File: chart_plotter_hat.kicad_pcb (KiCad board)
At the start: 4 copper layers, 65 x 56 mm, 37 parts, among them J1 Conn_02x03_Odd_Even, J2 Conn_01x04, J3 40HAT, J4 Conn_01x04, J5 Conn_01x04, J6 Conn_01x02, J7 Conn_01x04, J8 Conn_02x03_Odd_Even, Q1 DMG2305UX, Q2 DMMT5401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

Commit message: Added pulldown R10 on MCU_RUNNING
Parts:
- added R10: 10K, Resistors_SMD:R_0603, F.Cu at (112.0, 84.5)
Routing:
- net MCU_RUNNING: track 31.0 -> 32.3 mm
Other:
- board text added: "12V"
- board text added: "5V"
- board text removed: "+12V"
- board text removed: "+5V"

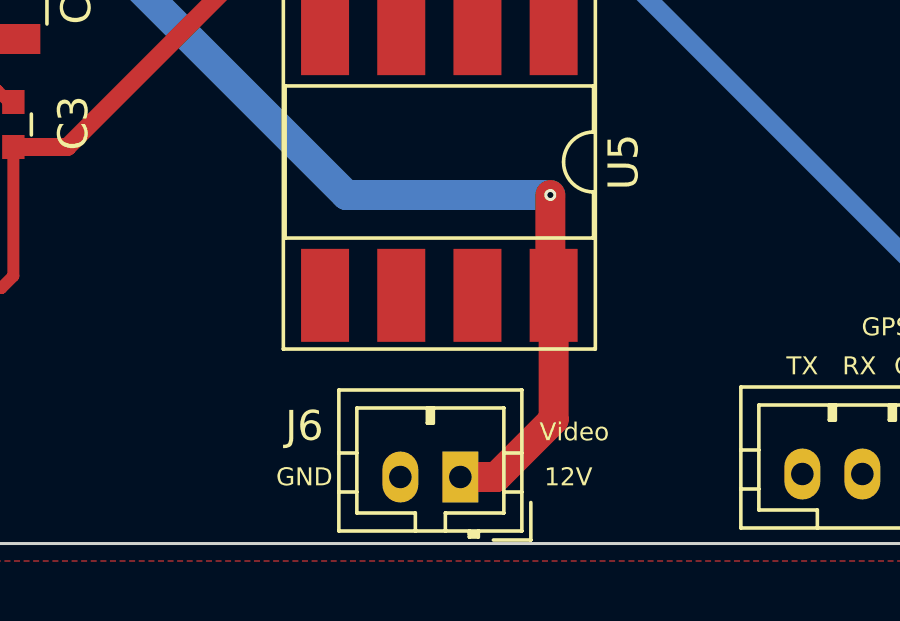
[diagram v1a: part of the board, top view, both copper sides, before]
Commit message: Fixed relay net
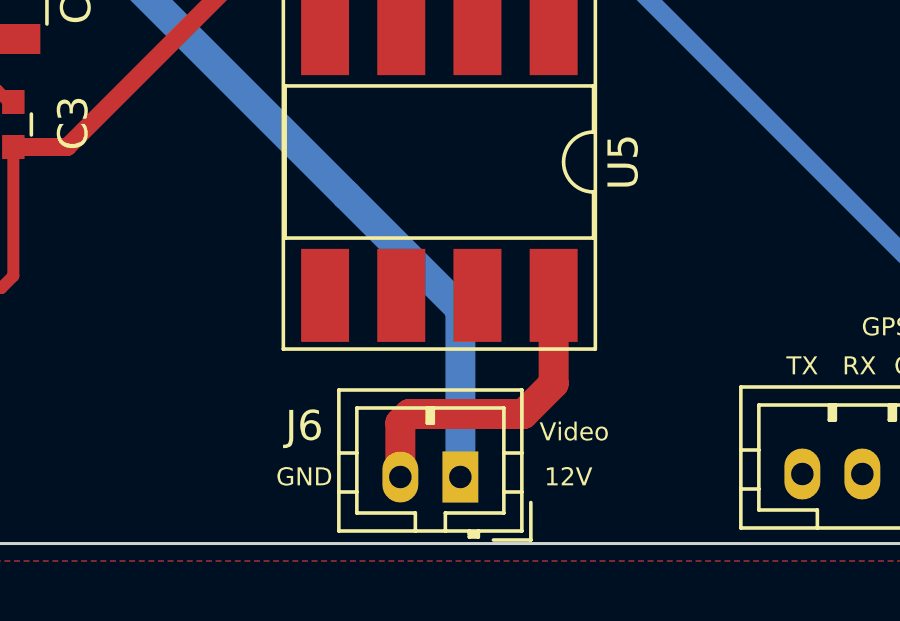
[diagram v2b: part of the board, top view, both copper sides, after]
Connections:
- J6 pad 2: GND -> Net-(J6-Pad2)
- U5 pad 8: +12V -> Net-(J6-Pad2)
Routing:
- net Net-(J6-Pad2): track 0.00 -> 10.6 mm
- net +12V: track 67.7 -> 60.4 mm, vias 2 -> 1

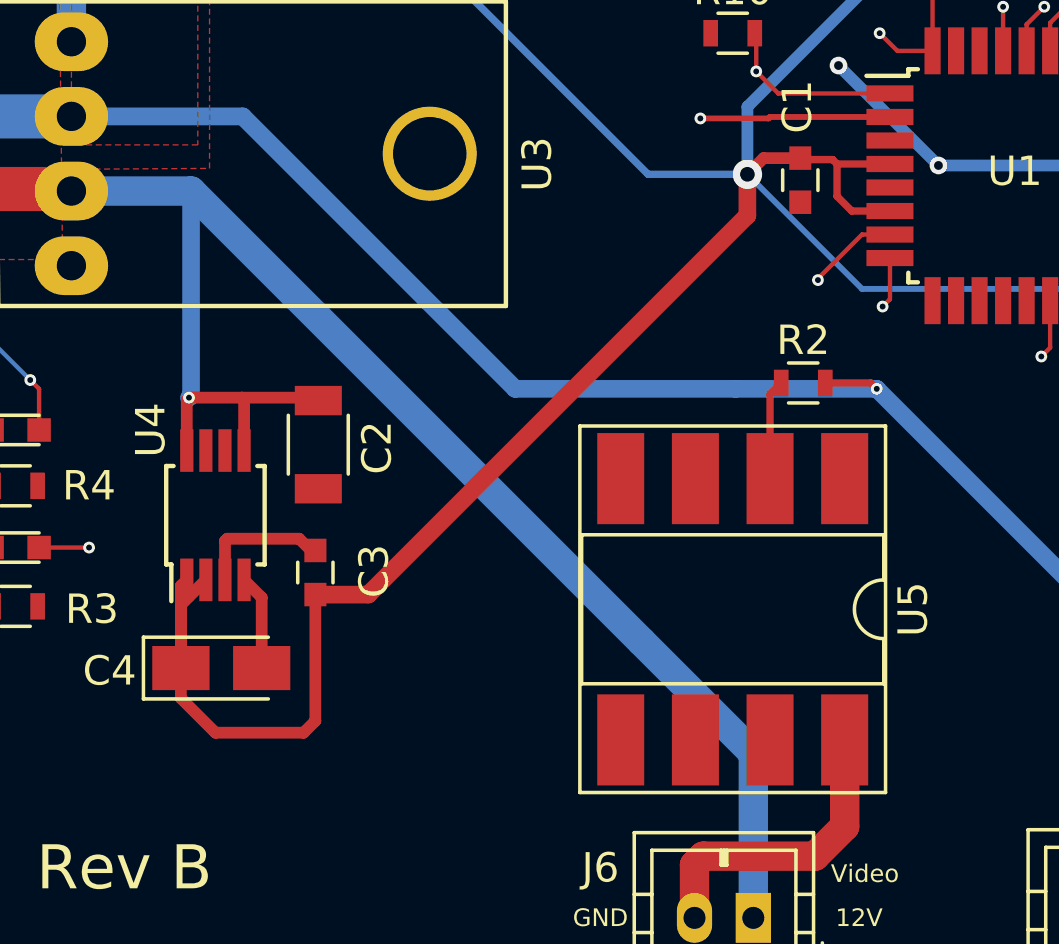
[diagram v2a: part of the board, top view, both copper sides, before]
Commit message: Moved R2 resistor to ground side of relay circuit
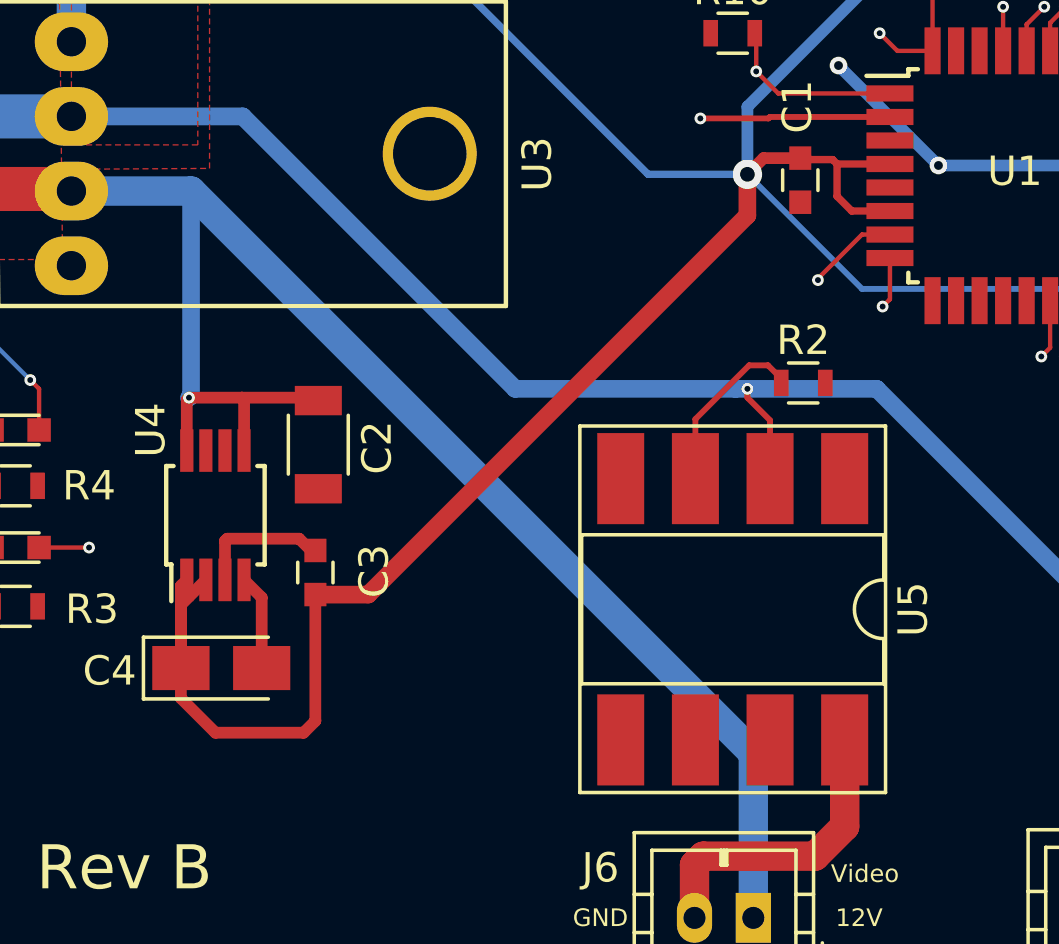
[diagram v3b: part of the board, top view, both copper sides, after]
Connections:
- R2 pad 2: /P5V -> GND
- U5 pad 2: Net-(R2-Pad1) -> /P5V
- U5 pad 3: GND -> Net-(R2-Pad1)
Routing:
- net Net-(R2-Pad1): track 3.41 -> 6.04 mm
- net /P5V: track 76.7 -> 78.3 mm

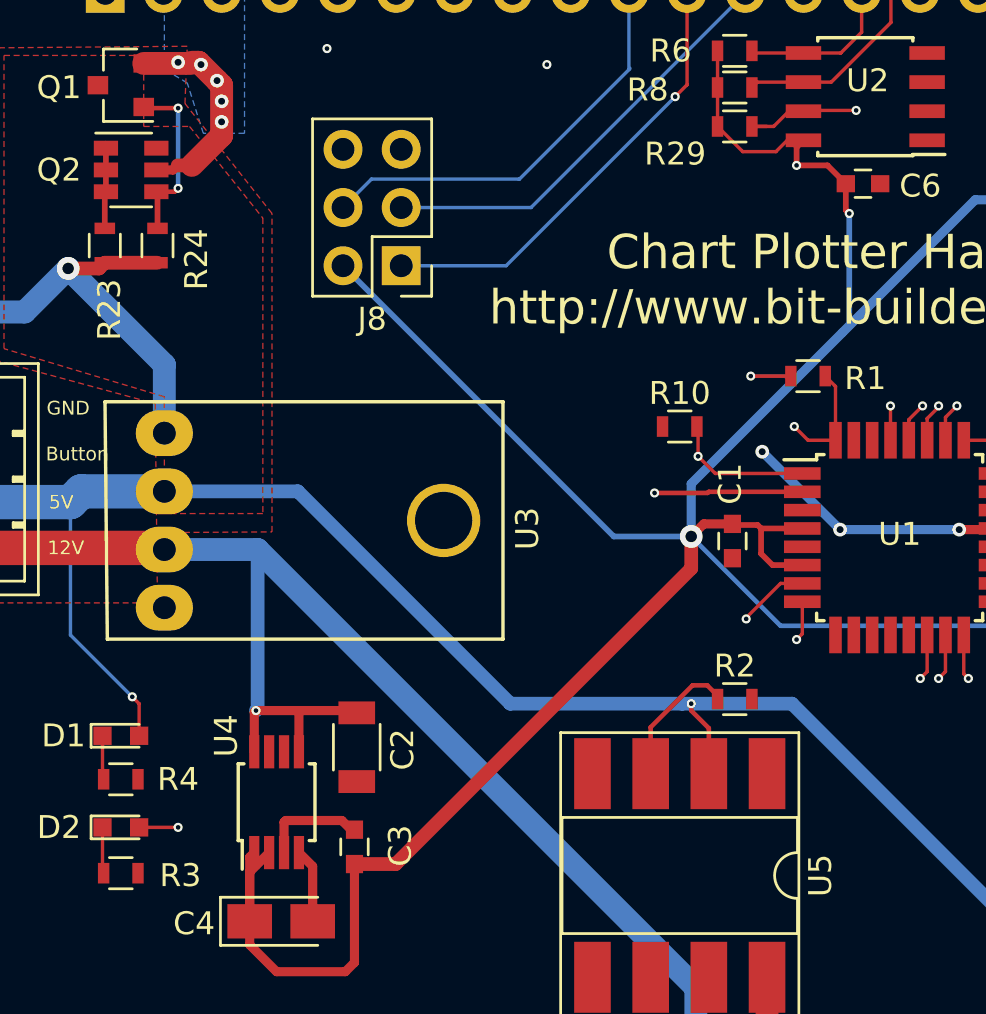
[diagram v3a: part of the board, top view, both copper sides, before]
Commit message: Moved second led to MISO instead of shutdown
Cleaned up some via's
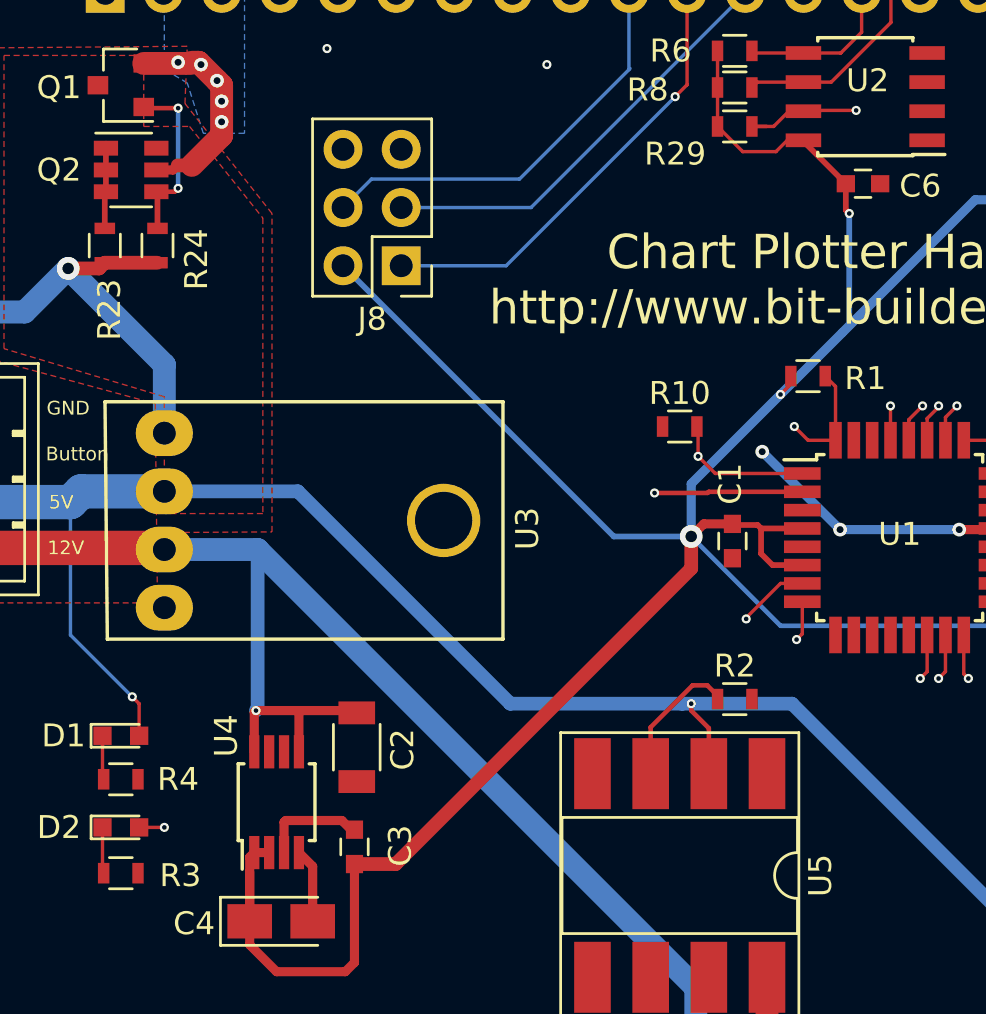
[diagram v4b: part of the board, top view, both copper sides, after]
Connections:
- D2 pad 2: SHUTDOWN -> MISO
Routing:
- net SHUTDOWN: track 64.8 -> 34.8 mm, vias 2 -> 1
- net MISO: track 56.7 -> 86.6 mm, vias 2 -> 3
- net +3V3: track 142.8 -> 138.5 mm, vias 5 -> 4

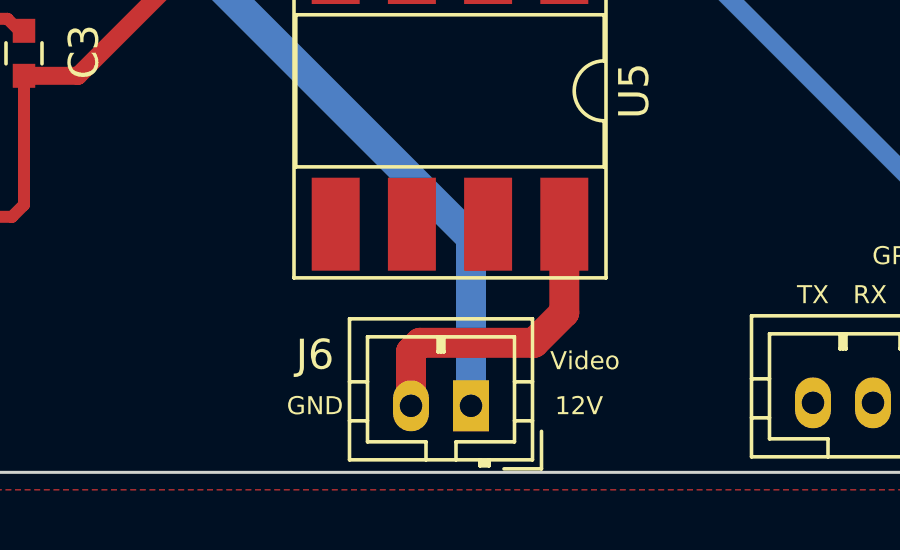
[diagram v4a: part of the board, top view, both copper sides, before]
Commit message: Redid relay wiring
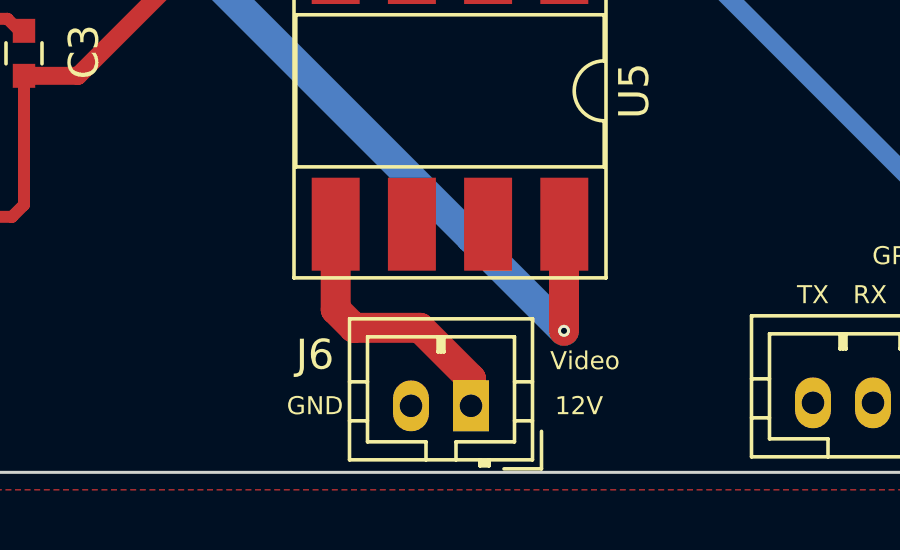
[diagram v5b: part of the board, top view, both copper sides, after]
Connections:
- J6 pad 1: +12V -> Net-(J6-Pad1)
- J6 pad 2: Net-(J6-Pad2) -> GND
- U5 pad 5: GND -> Net-(J6-Pad1)
- U5 pad 8: Net-(J6-Pad2) -> +12V
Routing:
- net Net-(J6-Pad2): track 10.6 -> 0.00 mm
- net Net-(J6-Pad1): track 0.00 -> 9.21 mm
- net +12V: track 60.4 -> 62.9 mm, vias 1 -> 2

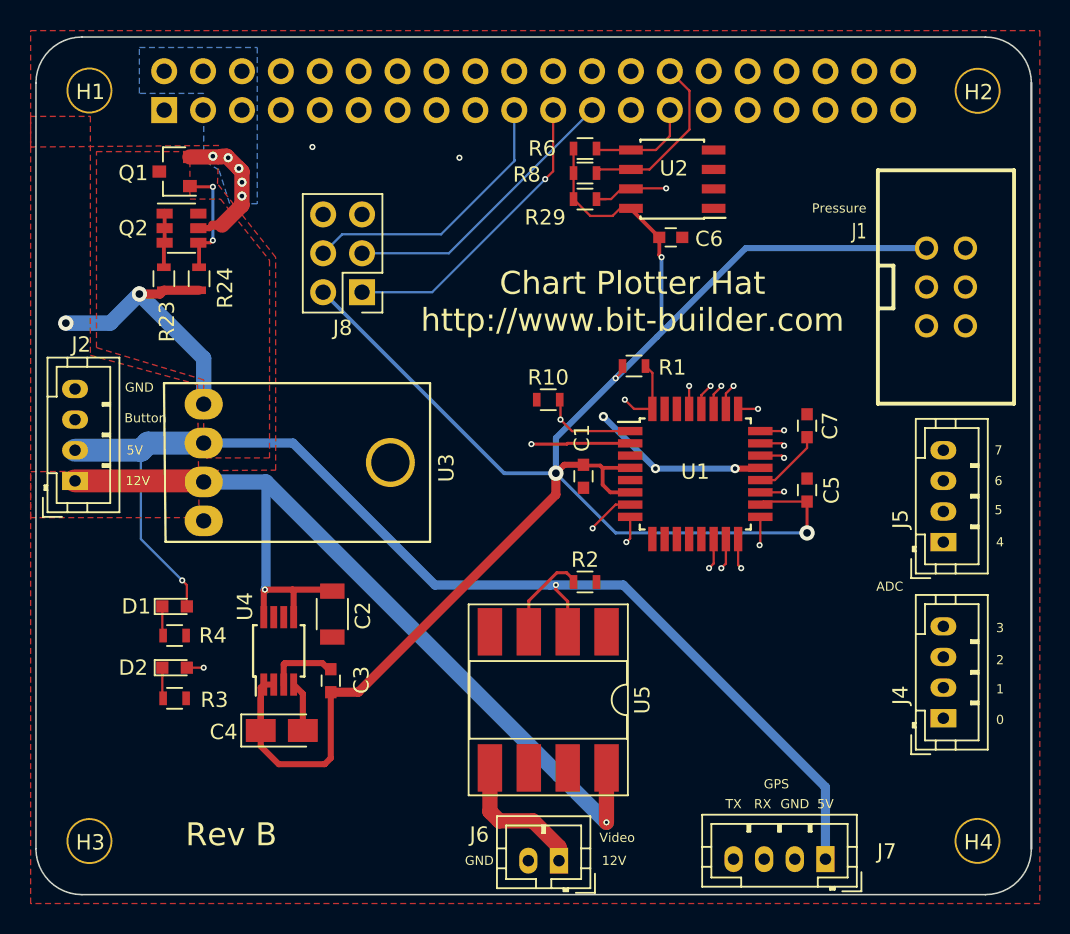
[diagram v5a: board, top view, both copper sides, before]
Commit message: Added voltmeter connection
Added reverse polarity protection diode
Moved non-power LED to it's own pin
Added R5, SHUTDOWN pull-down resistor
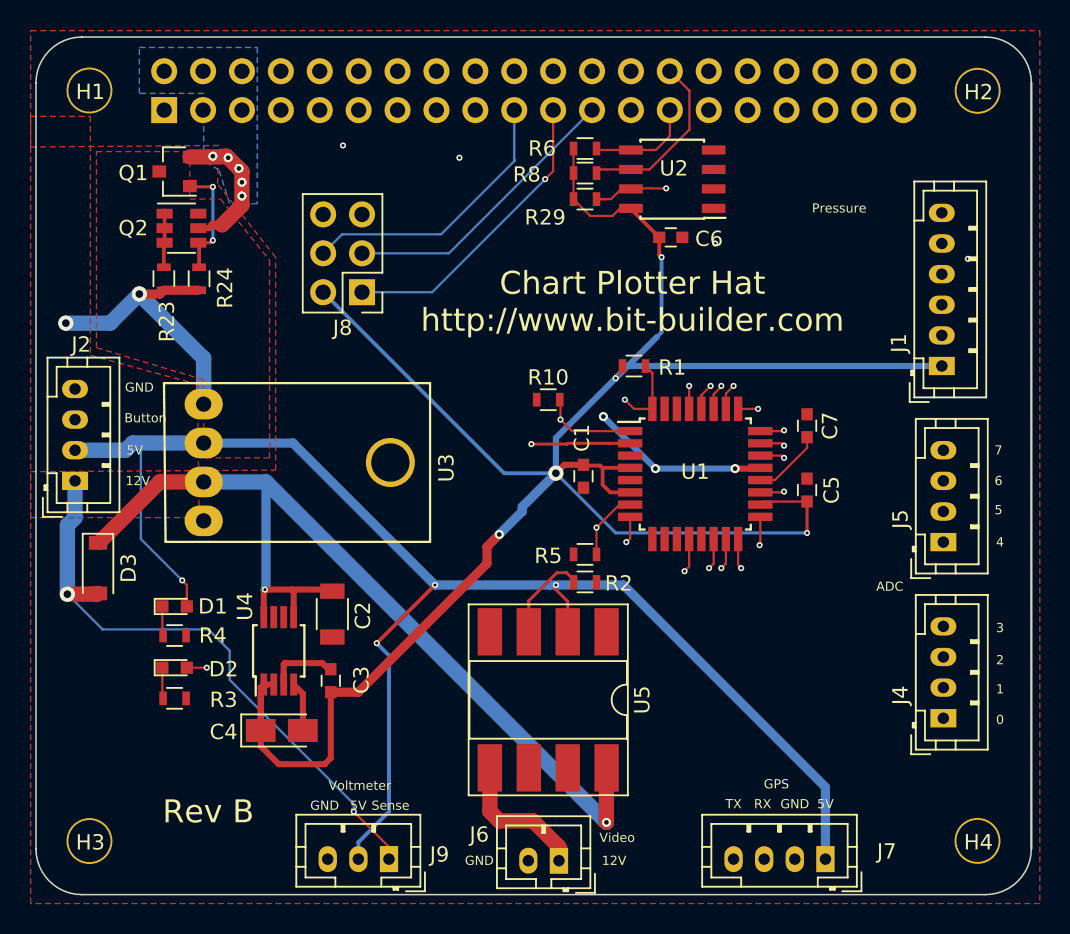
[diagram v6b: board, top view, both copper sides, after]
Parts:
- added D3: PMEG3020EH, Diodes_SMD:D_SOD-123, F.Cu at (82.6, 95.5)
- added J9: Conn_01x03, Connectors_JST:JST_PH_B3B-PH-K_03x2.00mm_Straight, F.Cu at (101.6, 114.5)
- added R5: 10K, Resistors_SMD:R_0603, F.Cu at (114.4, 94.6)
- C2: value 1uF -> 1uF (25V)
- J1: value Conn_02x03_Odd_Even -> Conn_01x06; footprint CustomComponents:BOX-HEADER6 -> Connectors_JST:JST_PH_B6B-PH-K_06x2.00mm_Straight
- moved J1 7.76 mm to (137.7, 82.3), turned to 90 degrees
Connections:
- D2 pad 2: MISO -> Net-(D2-Pad2)
- J2 pad 1: +12V -> /12VBAT
- U1 pad 12: (no net) -> Net-(D2-Pad2)
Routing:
- net /12VBAT: track 0.00 -> 39.7 mm, vias 0 -> 2
- net Net-(D2-Pad2): track 0.00 -> 37.3 mm, vias 0 -> 2
- net MISO: track 86.6 -> 56.7 mm, vias 3 -> 2
- net /P5V: track 78.3 -> 98.8 mm, vias 2 -> 4
- net EOC: track 47.7 -> 56.5 mm, vias 0 -> 1
- net SDA: track 56.8 -> 53.3 mm
- net SerialTX: track 65.4 -> 62.8 mm
- net SHUTDOWN: track 34.8 -> 36.6 mm
- net SCL: track 50.6 -> 49.4 mm, vias 0 -> 1
- net +3V3: track 138.5 -> 139.0 mm, vias 4 -> 5
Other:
- board text added: "Sense"
- board text added: "Voltmeter"
